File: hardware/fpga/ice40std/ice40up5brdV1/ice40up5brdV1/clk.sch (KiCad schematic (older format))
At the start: 2 parts, among them X1 ASE-xxxMHz

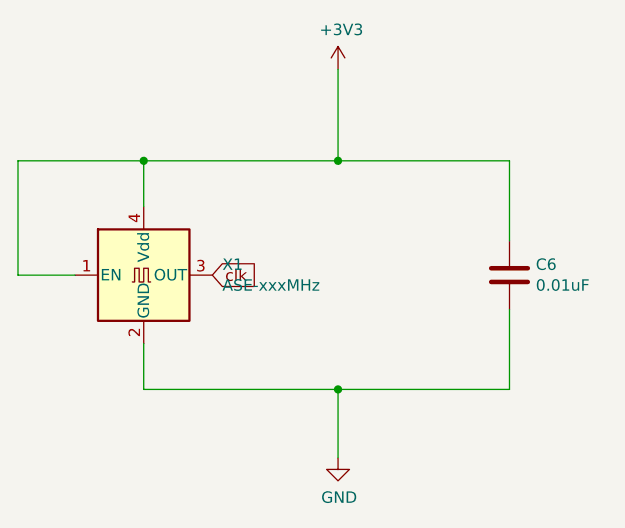
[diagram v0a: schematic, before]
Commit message: usb => mcu => ice40 fpga => NAND flash bridge started
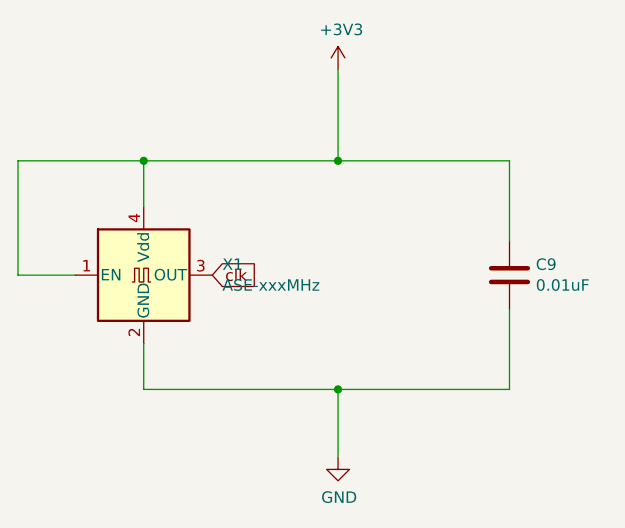
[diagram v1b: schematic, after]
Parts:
- renumbered C6 to C9
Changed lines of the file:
@@
 $EndComp
 $Comp
-L Device:C C6
+L Device:C C9
 U 1 1 60AB7231
 P 5250 3800
-F 0 "C6" H 5365 3846 50  0000 L CNN
+F 0 "C9" H 5365 3846 50  0000 L CNN
 F 1 "0.01uF" H 5365 3755 50  0000 L CNN
 F 2 "Capacitor_SMD:C_0402_1005Metric" H 5288 3650 50  0001 C CNN
@@
 $EndComp
 $Comp
-L power:GND #PWR013
+L power:GND #PWR024
 U 1 1 60AB7989
 P 4500 4600
-F 0 "#PWR013" H 4500 4350 50  0001 C CNN
+F 0 "#PWR024" H 4500 4350 50  0001 C CNN
 F 1 "GND" H 4505 4427 50  0000 C CNN
 F 2 "" H 4500 4600 50  0001 C CNN
@@
 Connection ~ 4500 4300
 $Comp
-L power:+3V3 #PWR012
+L power:+3V3 #PWR023
 U 1 1 60AB7CF6
 P 4500 2900
-F 0 "#PWR012" H 4500 2750 50  0001 C CNN
+F 0 "#PWR023" H 4500 2750 50  0001 C CNN
 F 1 "+3V3" H 4515 3073 50  0000 C CNN
 F 2 "" H 4500 2900 50  0001 C CNN
